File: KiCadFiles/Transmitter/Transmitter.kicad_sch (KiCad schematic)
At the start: 5 parts, among them J1 AM-Joystick, SW1 SW_Push, SW2 SW_Push, U1 NRF24L01_Breakout

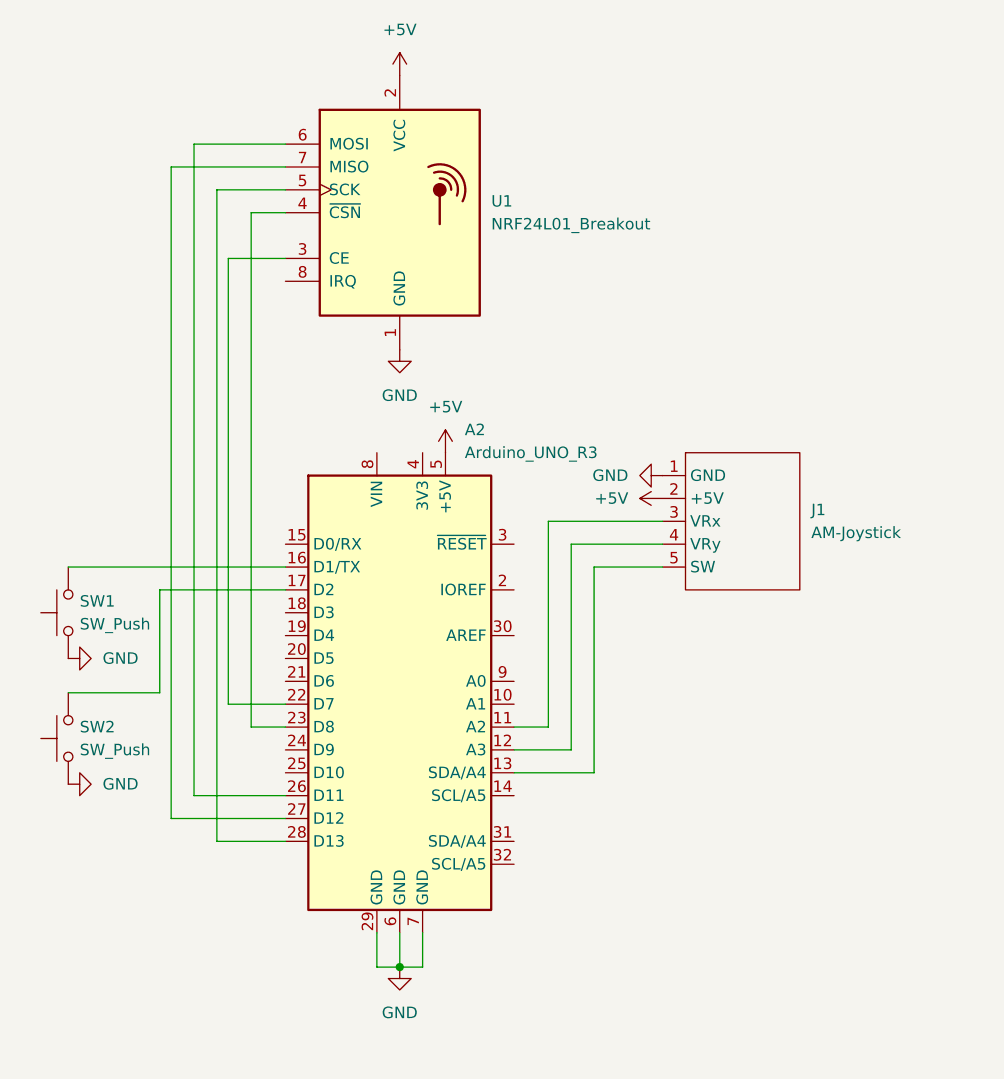
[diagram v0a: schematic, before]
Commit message: Add more buttons, update schematic, improve drive system
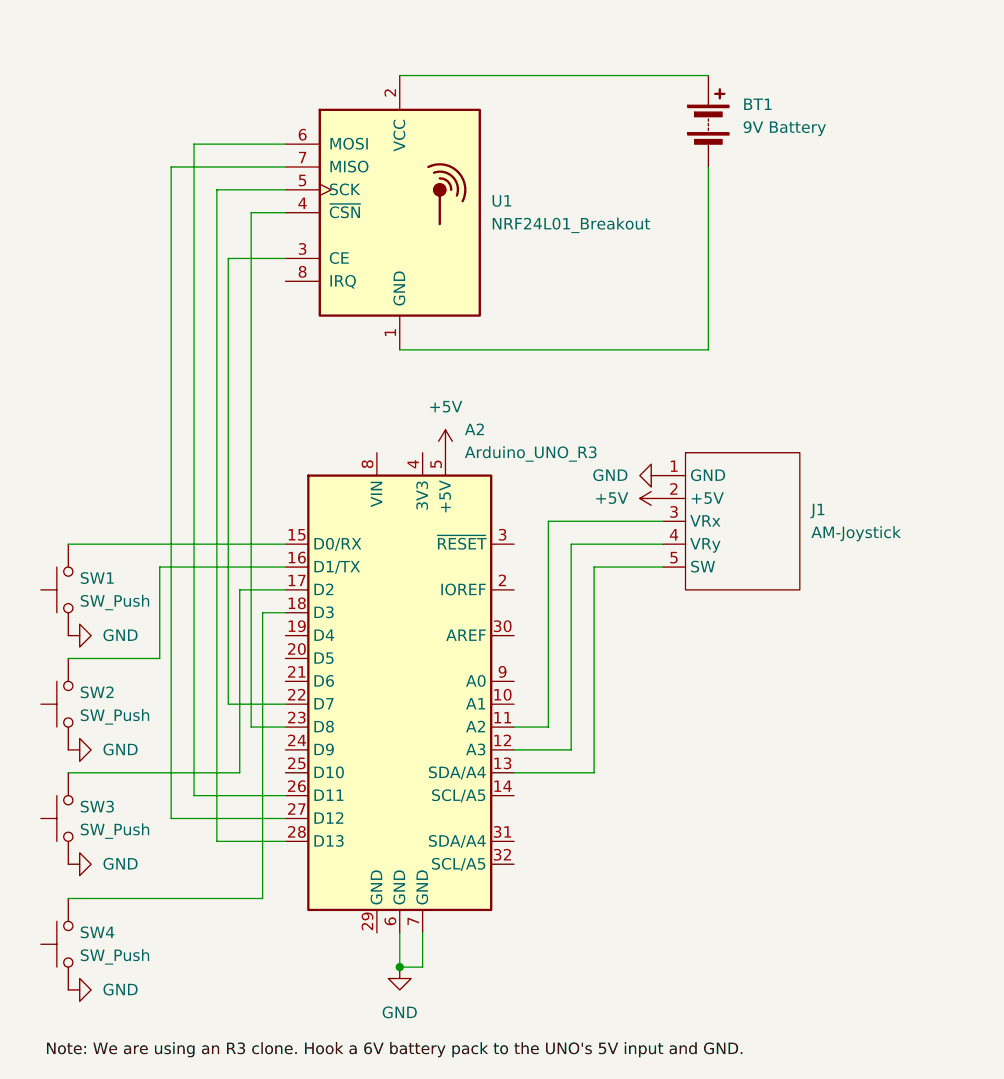
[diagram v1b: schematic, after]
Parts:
- added BT1: 9V Battery, symbol Device:Battery
- added SW3, SW4: SW_Push, symbol Switch:SW_Push
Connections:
- net +5V: no longer U1.2 (VCC)
- net GND: now also SW3.1, SW4.1; no longer A2.29 (GND), U1.1 (GND)
- net at A2.15 (D0/RX): now also SW1.2
- net at A2.16 (D1/TX): now also SW2.2; no longer SW1.2
- net at A2.17 (D2): now also SW3.2; no longer SW2.2
- net at A2.18 (D3): now also SW4.2
- new net: BT1.2 (-), U1.1 (GND)
- new net: BT1.1 (+), U1.2 (VCC)
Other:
- moved on the sheet: SW1, SW2

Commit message: Change button pins, schematic, and add quarter speed
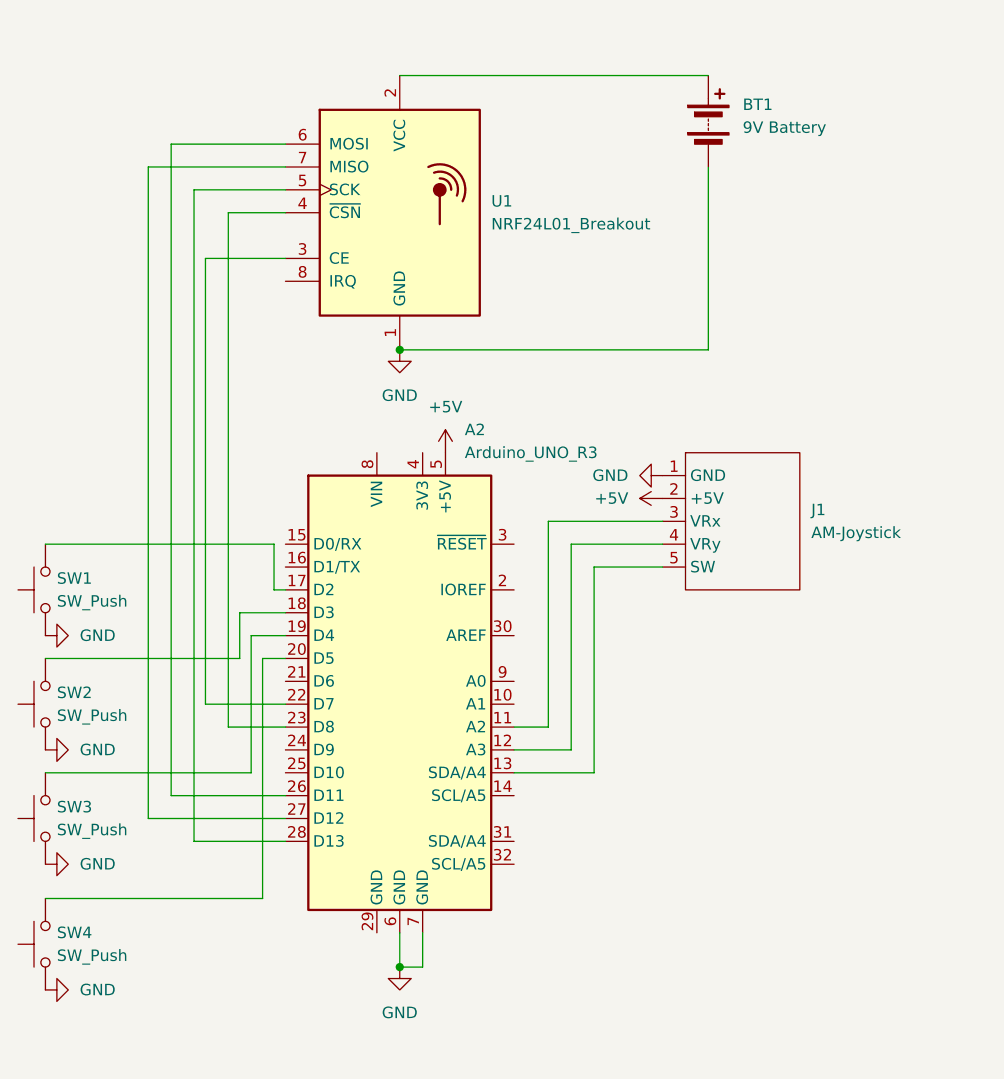
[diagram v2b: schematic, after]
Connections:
- net GND: now also BT1.2 (-), U1.1 (GND)
- net at SW3.2: now also A2.19 (D4); no longer A2.17 (D2)
- net at A2.15 (D0/RX): no longer SW1.2
- net at A2.16 (D1/TX): no longer SW2.2
- net at A2.18 (D3): now also SW2.2; no longer SW4.2
- net at A2.20 (D5): now also SW4.2
- new net: A2.17 (D2), SW1.2
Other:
- moved on the sheet: SW1, SW2, SW3, SW4
